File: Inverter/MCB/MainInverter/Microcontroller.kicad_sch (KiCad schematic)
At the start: 1 part, among them U7 Pico

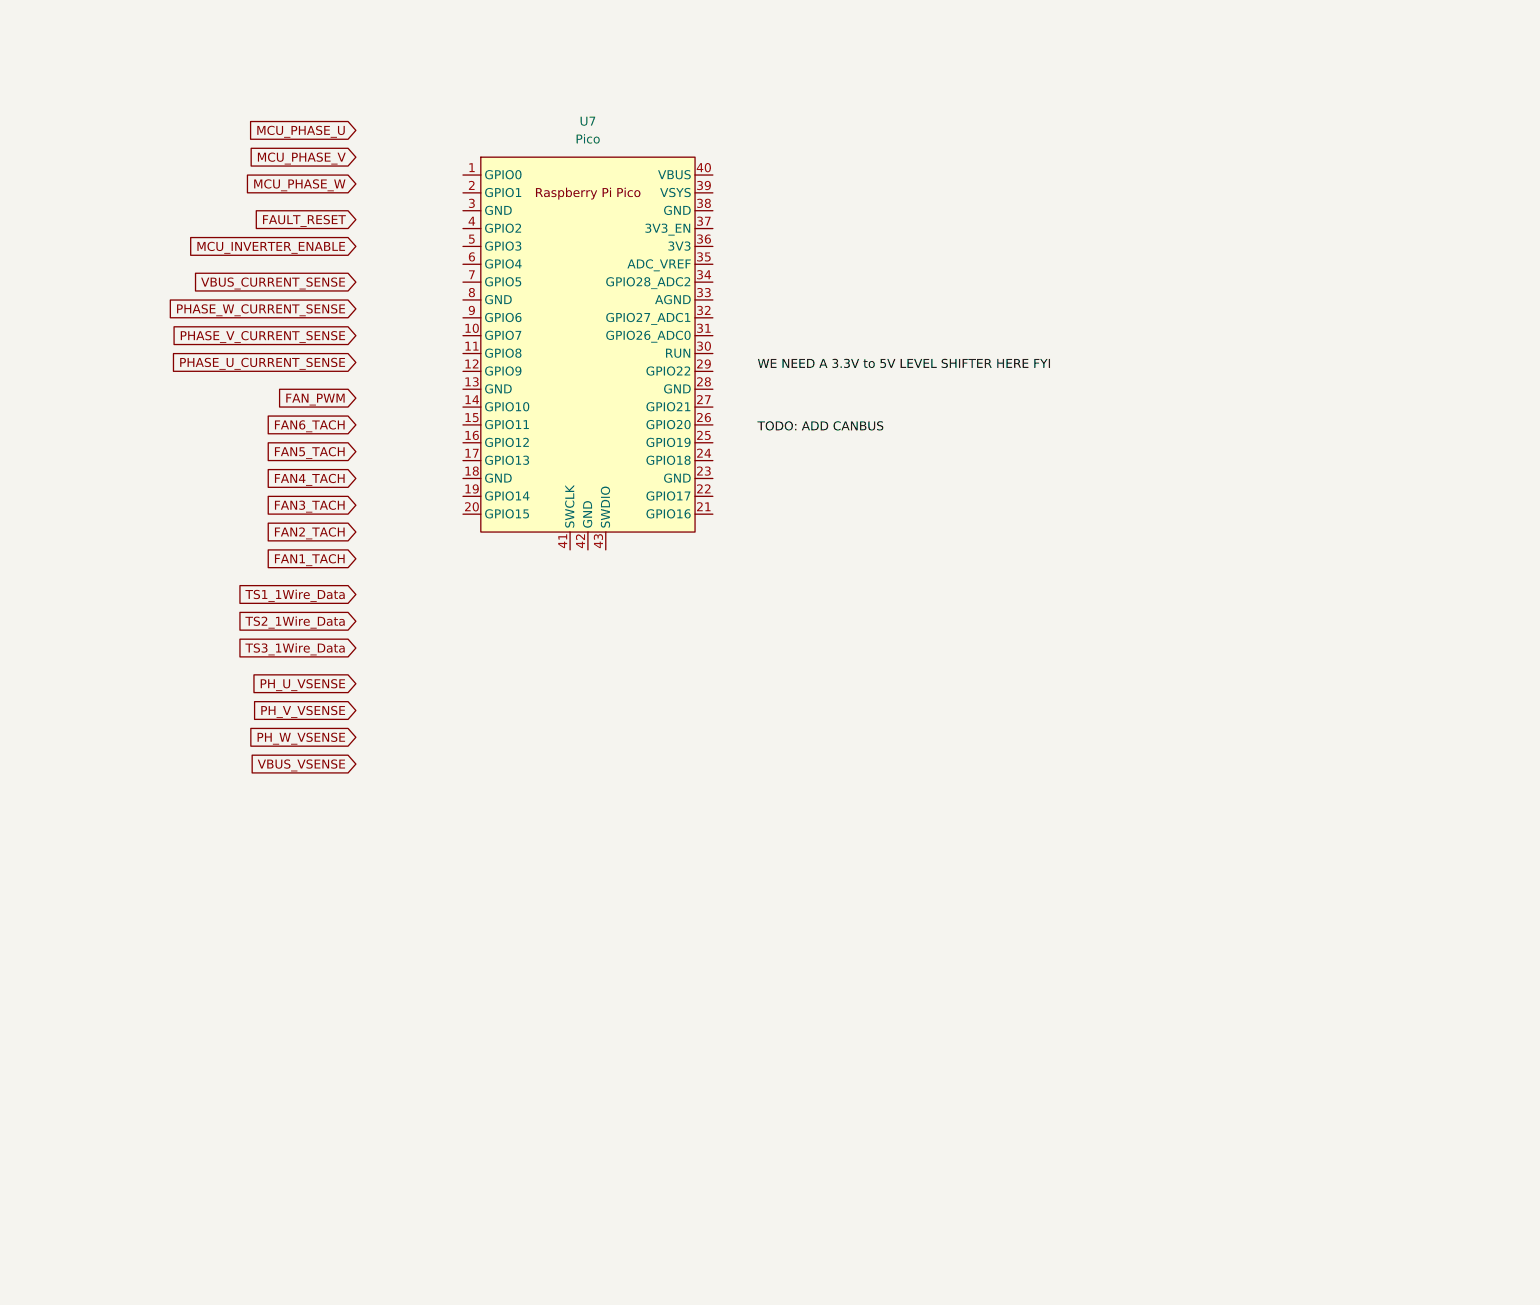
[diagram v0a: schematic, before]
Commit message: Update boost converter, add inverter
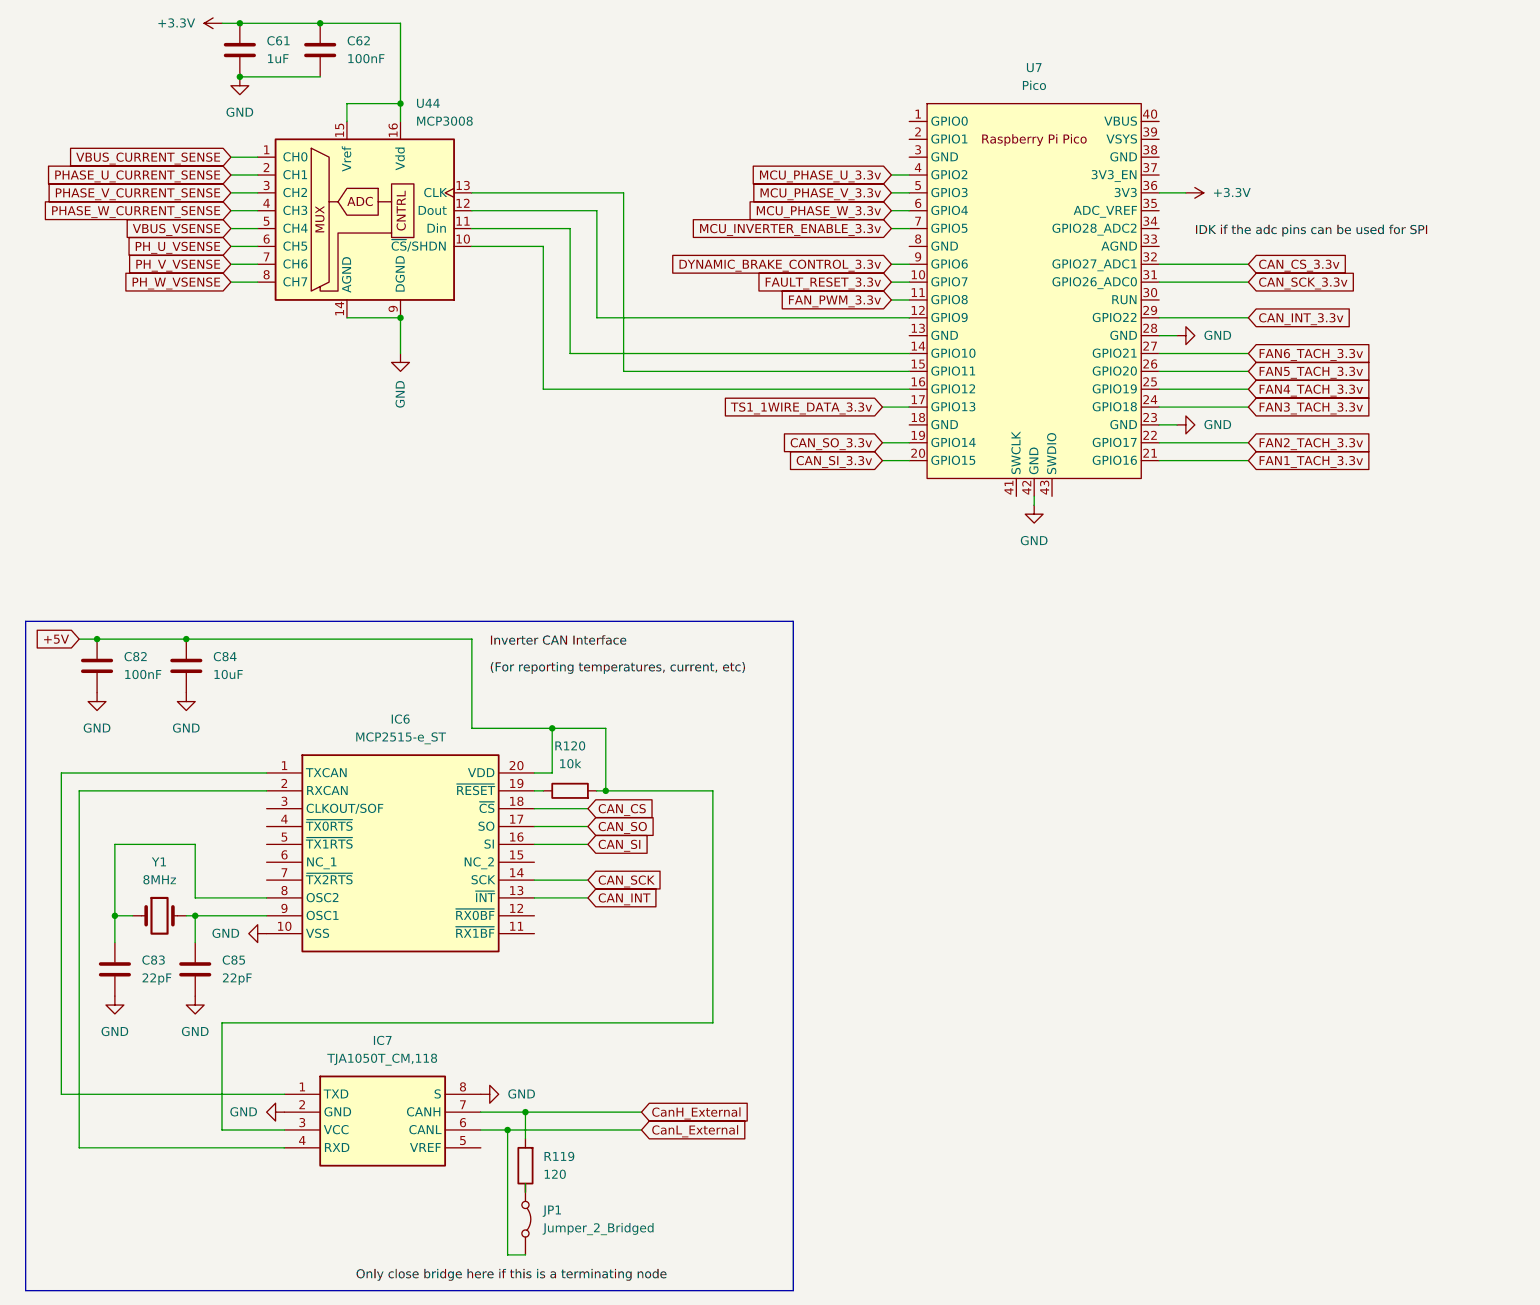
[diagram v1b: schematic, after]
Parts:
- added C61: 1uF, 1210, symbol Device:C
- added C62, C82: 100nF, 1210, symbol Device:C
- added C83, C85: 22pF, 1210, symbol Device:C
- added C84: 10uF, 1210, symbol Device:C
- added IC6: MCP2515-e_ST, SOP65P640X120-20N, symbol InverterCom:MCP2515-e_ST
- added IC7: TJA1050T_CM,118, SOIC127P600X175-8N, symbol InverterCom:TJA1050T_CM,118
- added JP1: Jumper_2_Bridged, symbol Jumper:Jumper_2_Bridged
- added R119: 120, 1210, symbol Device:R
- added R120: 10k, 1210, symbol Device:R
- added U44: MCP3008, symbol Analog_ADC:MCP3008
- added Y1: 8MHz, symbol Device:Crystal
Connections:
- net PHASE_U_CURRENT_SENSE: now also U44.2 (CH1)
- net PHASE_V_CURRENT_SENSE: now also U44.3 (CH2)
- net PHASE_W_CURRENT_SENSE: now also U44.4 (CH3)
- net PH_U_VSENSE: now also U44.6 (CH5)
- net PH_V_VSENSE: now also U44.7 (CH6)
- net PH_W_VSENSE: now also U44.8 (CH7)
- net VBUS_CURRENT_SENSE: now also U44.1 (CH0)
- net VBUS_VSENSE: now also U44.5 (CH4)
- net FAULT_RESET_3.3v: now reaches U7.10 (GPIO7)
- net FAN_PWM_3.3v: now reaches U7.11 (GPIO8)
- net at U7.12 (GPIO9): now also U44.12 (Dout)
- net at U7.14 (GPIO10): now also U44.11 (Din)
- net at U7.15 (GPIO11): now also U44.13 (CLK)
- net at U7.16 (GPIO12): now also U44.10 (~{CS}/SHDN)
- net TS1_1WIRE_DATA_3.3v: now reaches U7.17 (GPIO13)
- net CAN_SO_3.3v: now reaches U7.19 (GPIO14)
- net CAN_SI_3.3v: now reaches U7.20 (GPIO15)
- net FAN1_TACH_3.3v: now reaches U7.21 (GPIO16)
- net FAN2_TACH_3.3v: now reaches U7.22 (GPIO17)
- net GND: now reaches U7.23 (GND)
- net GND: now also U7.28 (GND), U7.42 (GND), C61.2, C62.2, C82.2, C83.2, C84.2, C85.2, IC6.10 (VSS), IC7.2 (GND), IC7.8 (S), U44.14 (AGND), U44.9 (DGND)
- net FAN3_TACH_3.3v: now reaches U7.24 (GPIO18)
- net FAN4_TACH_3.3v: now reaches U7.25 (GPIO19)
- net FAN5_TACH_3.3v: now reaches U7.26 (GPIO20)
- net FAN6_TACH_3.3v: now reaches U7.27 (GPIO21)
- net CAN_INT_3.3v: now reaches U7.29 (GPIO22)
- net CAN_SCK_3.3v: now reaches U7.31 (GPIO26_ADC0)
- net CAN_CS_3.3v: now reaches U7.32 (GPIO27_ADC1)
- net +3.3V: now reaches U7.36 (3V3)
- net +3.3V: now also C61.1, C62.1, U44.15 (Vref), U44.16 (Vdd)
- net MCU_PHASE_U_3.3v: now reaches U7.4 (GPIO2)
- net MCU_PHASE_V_3.3v: now reaches U7.5 (GPIO3)
- net MCU_PHASE_W_3.3v: now reaches U7.6 (GPIO4)
- net MCU_INVERTER_ENABLE_3.3v: now reaches U7.7 (GPIO5)
- net DYNAMIC_BRAKE_CONTROL_3.3v: now reaches U7.9 (GPIO6)
- new net: C83.1, IC6.8 (OSC2), Y1.1
- new net: C85.1, IC6.9 (OSC1), Y1.2
- new net: JP1.1 (A), R119.1
- new net: IC6.1 (TXCAN), IC7.1 (TXD)
- new net: IC6.19 (~{RESET}), R120.1
- new net: IC6.2 (RXCAN), IC7.4 (RXD)
- new net +5V: C82.1, C84.1, IC6.20 (VDD), IC7.3 (VCC), R120.2
- new net CAN_CS: IC6.18 (~{CS})
- new net CAN_INT: IC6.13 (~{INT})
- new net CAN_SCK: IC6.14 (SCK)
- new net CAN_SI: IC6.16 (SI)
- new net CAN_SO: IC6.17 (SO)
- new net CanH_External: IC7.7 (CANH), R119.2
- new net CanL_External: IC7.6 (CANL), JP1.2 (B)
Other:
- moved on the sheet: U7
